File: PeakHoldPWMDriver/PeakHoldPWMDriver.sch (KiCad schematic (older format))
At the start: 66 parts, among them Q1 BSP78, Q16 SMD-MOSFET-N-CH-55V-2.1A-AO34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, Q17 AO3401A, Q19 SMD-MOSFET-N-CH-55V-2.1A-AO34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, Q2 BSP78, Q20 AO3401A, Q21 SMD-MOSFET-N-CH-55V-2.1A-AO34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, Q22 SMD-MOSFET-N-CH-55V-2.1A-AO34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, Q23 AO3401A, Q24 AO3401A, Q3 BSP78, Q4 BSP78, U1 LM2901, U3 LM78M05_TO220, U5 TL431DBZ

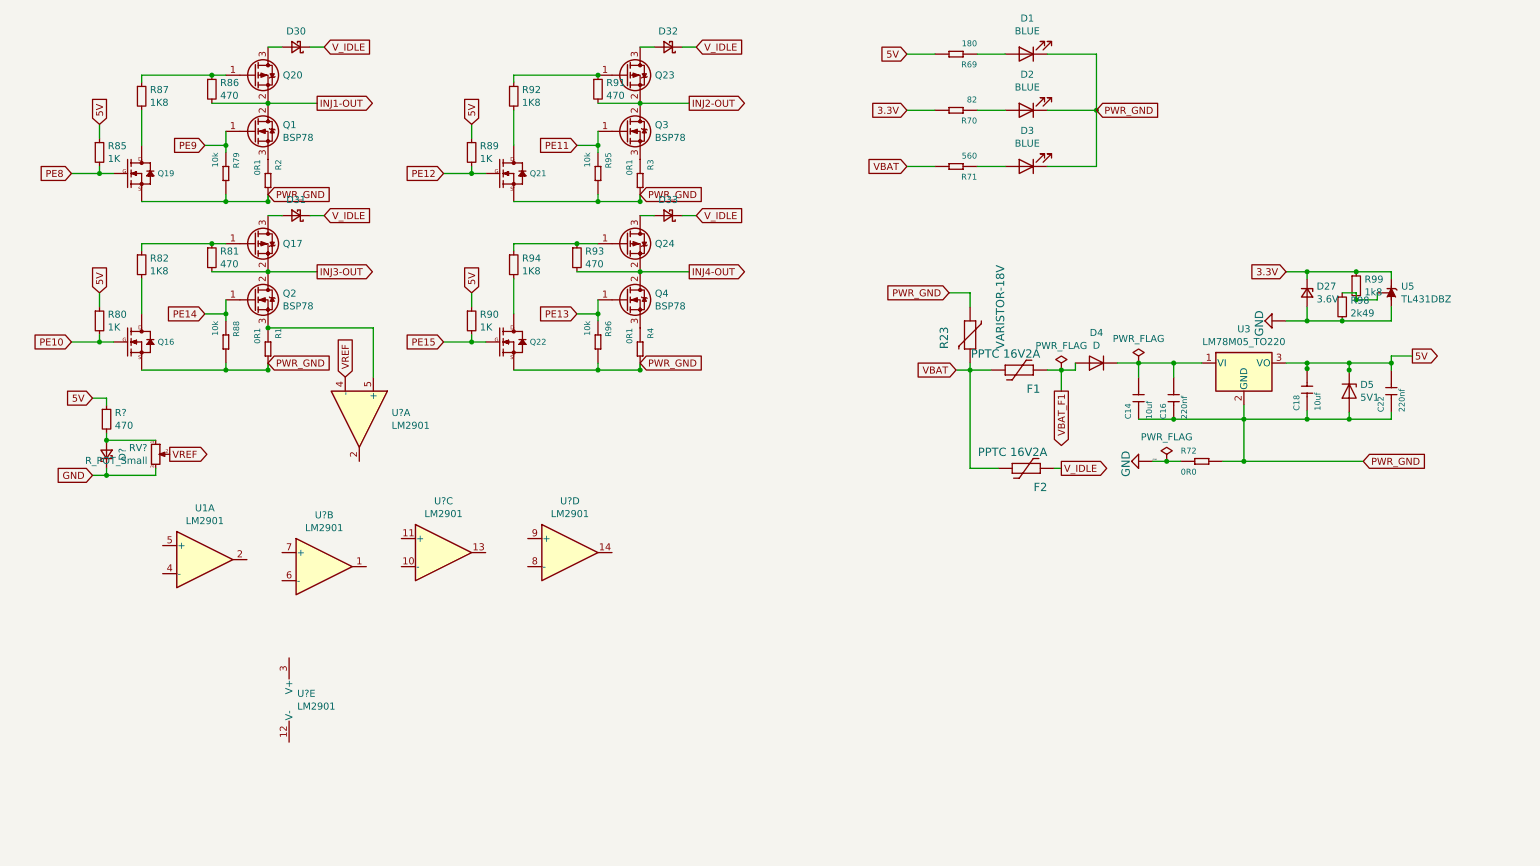
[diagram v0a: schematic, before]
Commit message: Stared implementing peak and hold driver. Also started in V0.6 of my board where the peak and hold driver is included
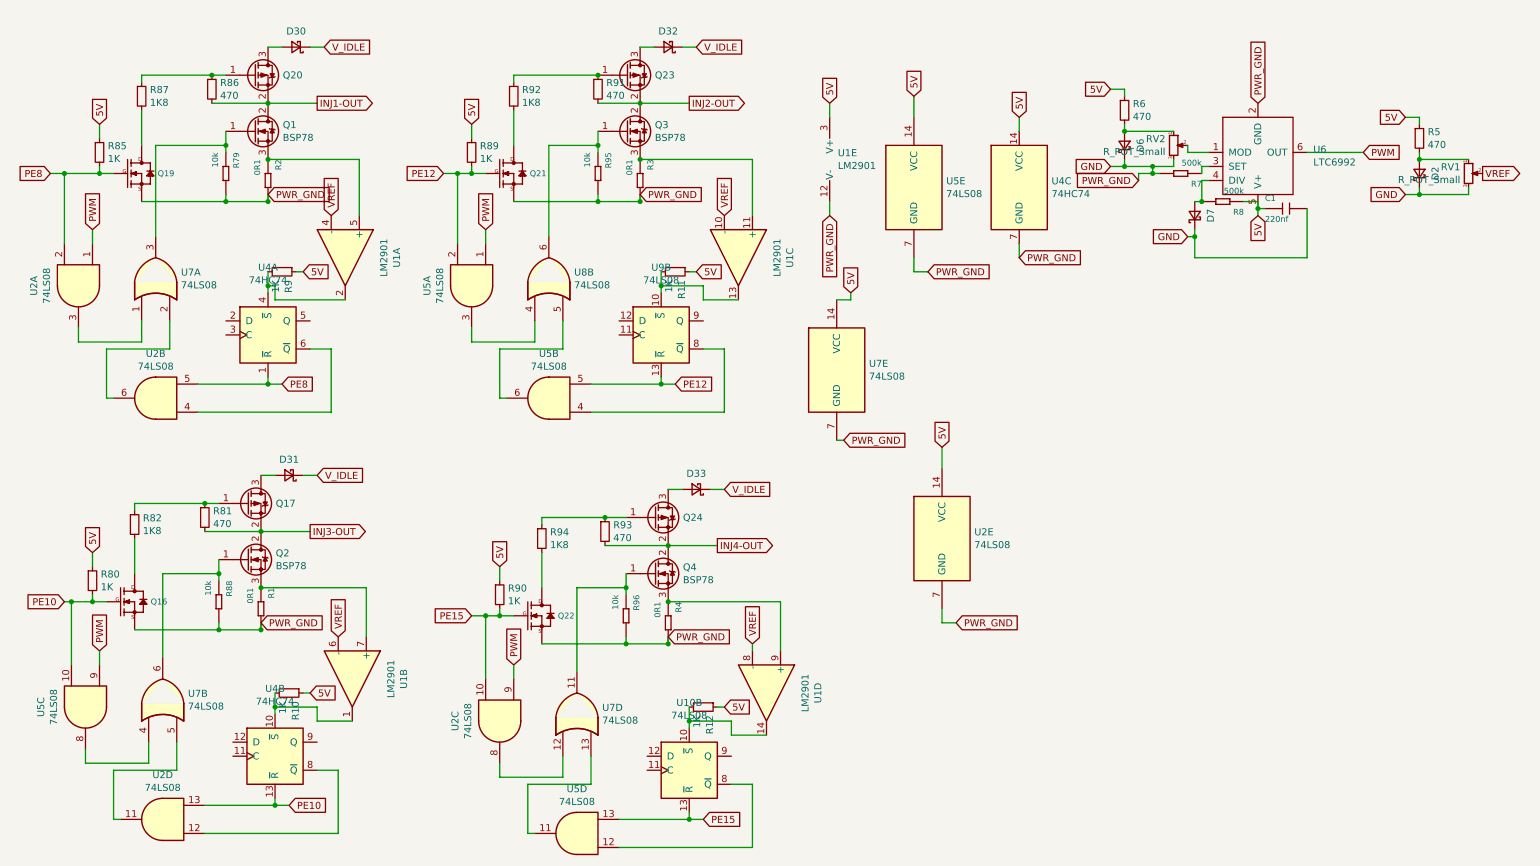
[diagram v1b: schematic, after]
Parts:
- removed C14, C18: 10uf, Capacitor_SMD:C_1206_3216Metric, symbol Speeduino_base-eagle-import:CERAMIC-10UF-25V-10%-X5R(1206)
- removed C16, C22: 220nf, Capacitor_SMD:C_0603_1608Metric_Pad1.05x0.95mm_HandSolder, symbol Speeduino_base-eagle-import:CERAMIC-220NF-25V-10%-X7R(0603)
- removed D1, D2, D3: BLUE, LED_SMD:LED_0603_1608Metric_Pad1.05x0.95mm_HandSolder, symbol Device:LED
- removed D27: 3.6V, Diode_SMD:D_MiniMELF_Handsoldering, symbol Device:D_Zener_Small
- removed D4: D, Diode_SMD:D_SMA_Handsoldering, symbol Device:D
- removed D5: 5V1, Diode_SMD:D_1206_3216Metric_Pad1.42x1.75mm_HandSolder, symbol Device:D_Zener
- removed F1, F2: PPTC 16V2A, Resistor_SMD:R_1812_4532Metric_Pad1.30x3.40mm_HandSolder, symbol Speeduino_base-eagle-import:?1812L
- removed R23: VARISTOR-18V, Varistor:RV_Disc_D12mm_W3.9mm_P7.5mm, symbol Speeduino_base-eagle-import:VARISTOR-7,5
- removed R69: 180, Resistor_SMD:R_0603_1608Metric_Pad1.05x0.95mm_HandSolder, symbol Speeduino_base-eagle-import:SMD-RES-470R-5%-1_10W(0603)
- removed R70: 82, Resistor_SMD:R_0603_1608Metric_Pad1.05x0.95mm_HandSolder, symbol Speeduino_base-eagle-import:SMD-RES-470R-5%-1_10W(0603)
- removed R71: 560, Resistor_SMD:R_0603_1608Metric_Pad1.05x0.95mm_HandSolder, symbol Speeduino_base-eagle-import:SMD-RES-470R-5%-1_10W(0603)
- removed R72: 0R0, Resistor_SMD:R_0603_1608Metric_Pad1.05x0.95mm_HandSolder, symbol Speeduino_base-eagle-import:SMD-RES-470R-5%-1_10W(0603)
- removed R98: 2k49, Resistor_SMD:R_0603_1608Metric_Pad1.05x0.95mm_HandSolder, symbol Device:R_Small
- removed R99: 1k8, Resistor_SMD:R_0603_1608Metric_Pad1.05x0.95mm_HandSolder, symbol Device:R_Small
- removed U3: LM78M05_TO220, Package_TO_SOT_THT:TO-220-3_Vertical, symbol Regulator_Linear:LM78M05_TO220
- removed U5: TL431DBZ, Package_TO_SOT_SMD:SOT-23, symbol Reference_Voltage:TL431DBZ
- removed U?: LM2901, Package_SO:TSSOP-14_4.4x5mm_P0.65mm, symbol Comparator:LM2901
- added C1: 220nf, Capacitor_SMD:C_0603_1608Metric_Pad1.05x0.95mm_HandSolder, symbol Speeduino_base-eagle-import:CERAMIC-220NF-25V-10%-X7R(0603)
- added D6, D7: SS310, Diode_SMD:D_SMA-SMB_Universal_Handsoldering, symbol Device:D_Schottky_Small
- added R10, R11, R12, R9: 1K, Resistor_SMD:R_0603_1608Metric_Pad1.05x0.95mm_HandSolder, symbol Device:R_Small
- added R6: 470, Resistor_SMD:R_0603_1608Metric_Pad1.05x0.95mm_HandSolder, symbol Device:R_Small
- added R7, R8: 500k, Resistor_SMD:R_0603_1608Metric_Pad1.05x0.95mm_HandSolder, symbol Speeduino_base-eagle-import:SMD-RES-470R-5%-1_10W(0603)
- added RV2: R_POT_Small, Potentiometer_SMD:Potentiometer_Bourns_3314R-1_Vertical_Hole, symbol Device:R_POT_Small
- added U10, U9: 74LS08, Package_SO:SO-14_5.3x10.2mm_P1.27mm, symbol 74xx:74HC74
- added U2, U5: 74LS08, Package_SO:SO-14_5.3x10.2mm_P1.27mm, symbol 74xx:74LS08
- added U4: 74HC74, Package_SO:SO-14_5.3x10.2mm_P1.27mm, symbol 74xx:74HC74
- added U6: LTC6992, Package_TO_SOT_SMD:SOT-23-6_Handsoldering, symbol speeduino_lib:LTC6992
- added U7, U8: 74LS08, Package_SO:SO-14_5.3x10.2mm_P1.27mm, symbol 74xx:74LS32
- Q17, Q20, Q23, Q24: value AO3401A -> TSM2309CX
- R1, R2, R3, R4: footprint Resistor_SMD:R_1206_3216Metric_Pad1.42x1.75mm_HandSolder -> Resistor_SMD:R_2512_6332Metric_Pad1.52x3.35mm_HandSolder
- RV1: renamed from RV?; footprint (none) -> Potentiometer_SMD:Potentiometer_Bourns_3314R-1_Vertical_Hole
- U1: footprint Package_SO:TSSOP-14_4.4x5mm_P0.65mm -> Package_SO:SO-14_5.3x10.2mm_P1.27mm
- U1: renamed from U?; footprint Package_SO:TSSOP-14_4.4x5mm_P0.65mm -> Package_SO:SO-14_5.3x10.2mm_P1.27mm
- gave numbers to parts that had none: 2
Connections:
- net PWR_GND is gone; now on net GND: Q16.2 (S), Q19.2 (S), Q21.2 (S), Q22.2 (S), R1.2, R2.2, R3.2, R4.2, R79.2, R88.2, R95.2, R96.2
- net 5V: now also U1.3 (V+), C1.1, R10.1, R11.1, R12.1, R6.1, R8.1, R9.1, U2.14 (VCC), U4.14 (VCC), U5.14 (VCC), U6.5 (V+), U7.14 (VCC)
- net GND: now also U1.12 (V-), C1.2, D6.1 (K), D7.1 (K), R7.2, RV2.3, U2.7 (GND), U4.7 (GND), U5.7 (GND), U6.2 (GND), U7.7 (GND)
- net PE10: now also U2.13, U4.13 (~R), U5.10
- net PE12: now also U5.2, U5.5, U9.13 (~R)
- net PE15: now also U10.13 (~R), U2.10, U5.13
- net PE8: now also U2.2, U2.5, U4.1 (~R)
- net VREF: now also U1.10 (-), U1.4 (-), U1.6 (-), U1.8 (-)
- net at U1.2: now also R9.2, U4.4 (~S)
- net at U1.5 (+): now also Q1.3 (S), R2.1
- net at Q2.3 (S), R1.1: now also U1.7 (+)
- net at Q4.3 (S), R4.1: now also U1.9 (+)
- net at Q3.3 (S), R3.1: now also U1.11 (+)
- net at U1.1: now also R10.2, U4.10 (~S)
- net at U1.13: now also R11.2, U9.10 (~S)
- net at U1.14: now also R12.2, U10.10 (~S)
- net PE11: no longer names the net of Q3.1 (G), R95.1
- net PE11: now also U8.6
- net PE13: no longer names the net of Q4.1 (G), R96.1
- net PE13: now also U7.11
- net PE14: no longer names the net of Q2.1 (G), R88.1
- net PE14: now also U7.6
- net PE9: no longer names the net of Q1.1 (G), R79.1
- net PE9: now also U7.3
- new net: RV2.2, U6.1 (MOD)
- new net: R7.1, U6.3 (SET)
- new net: D7.2 (A), R8.2, U6.4 (DIV)
- new net: D6.2 (A), R6.2, RV2.1
- new net: U2.4, U4.6 (~Q)
- new net: U2.12, U4.8 (~Q)
- new net: U5.8, U7.4
- new net: U2.6, U7.2
- new net: U2.3, U7.1
- new net: U2.11, U7.5
- new net: U5.4, U9.8 (~Q)
- new net: U5.3, U8.4
- new net: U5.6, U8.5
- new net: U2.8, U7.12
- new net: U5.11, U7.13
- new net: U10.8 (~Q), U5.12
- new net PWM: U2.1, U2.9, U5.1, U5.9, U6.6 (OUT)
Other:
- moved on the sheet: D2, D31, D33, Q16, Q17, Q2, Q22, Q24, Q4, R1, R4, R5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
